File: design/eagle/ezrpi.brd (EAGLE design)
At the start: 65 x 56 mm, 40 parts, among them X1 26MHz, X2 32.768kHz, X3 48MHz

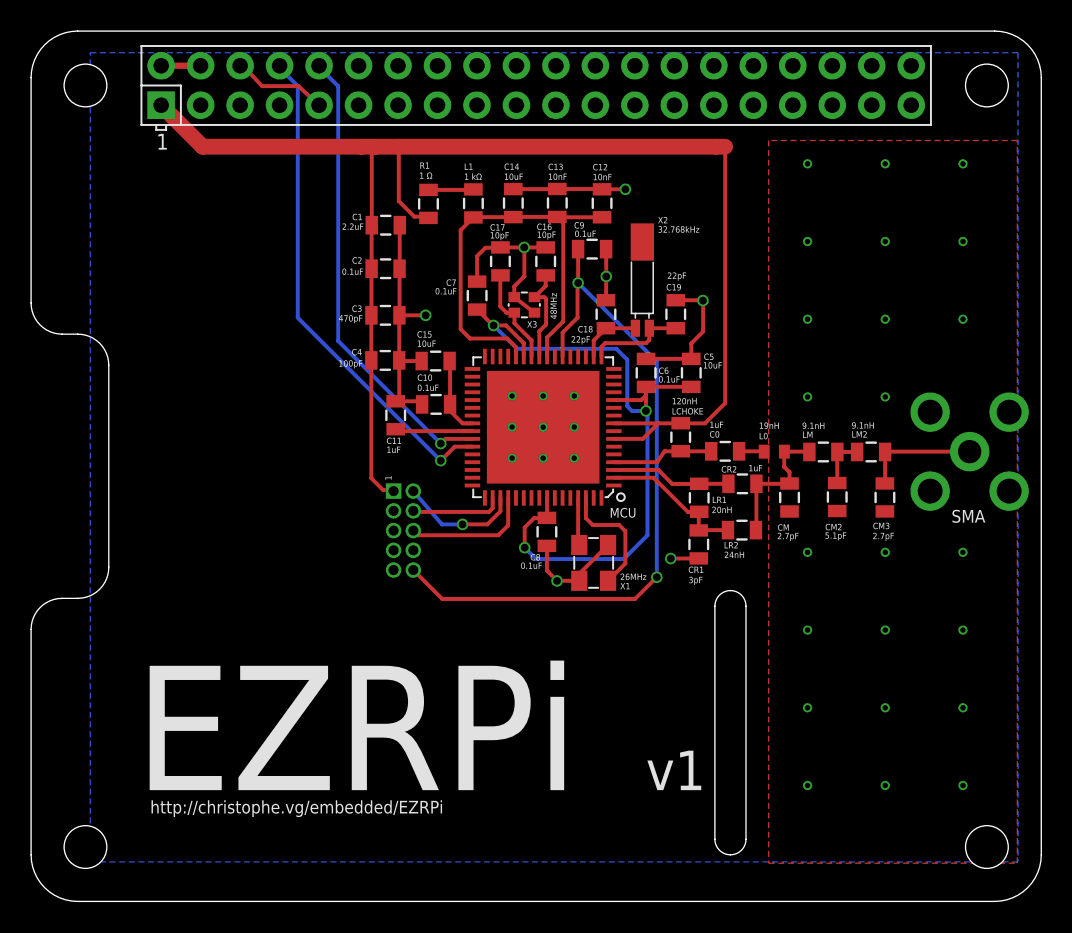
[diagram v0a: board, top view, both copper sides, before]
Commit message: added LEDs, improved traces, 50 Ω line, added vias
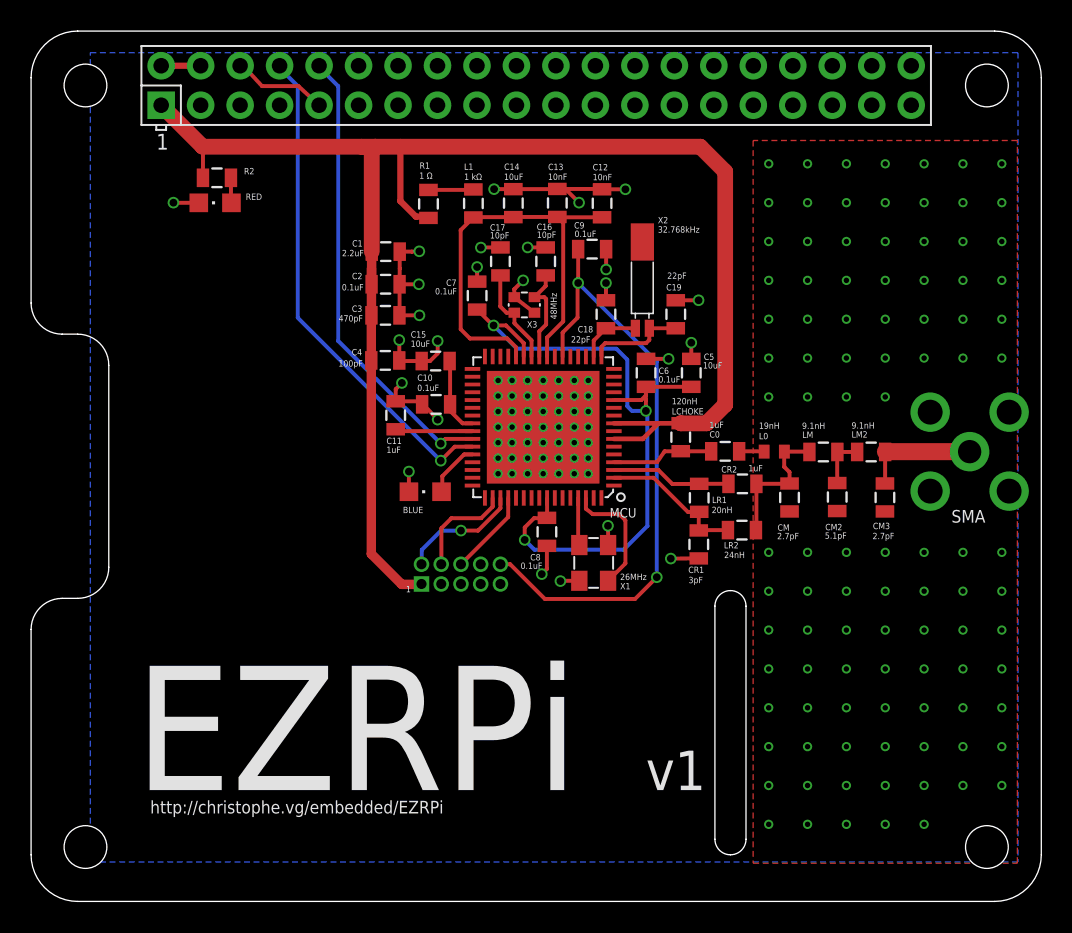
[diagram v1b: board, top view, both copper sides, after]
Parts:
- added BLUE, RED: (no value), led:CHIPLED_0805
- added R2: 68 Ω, passive:0805
- moved SWD 4.64 mm to (30.2, 23.6), turned to 0 degrees
- moved C1 1.70 mm to (25.4, 44.4)
- moved C2 1.00 mm to (25.4, 42.2)
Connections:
- new net LED-STATUS: BLUE.A, MCU.44
- new net N$8: R2.2, RED.A
- net GND: now also BLUE.C, RED.C
- net VCC: now also R2.1
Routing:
- net VCC: track 94.2 -> 109.5 mm
- net GND: track 62.2 -> 56.2 mm, vias 39 -> 174
- net RESET: track 45.4 -> 39.9 mm
- net LED-STATUS: track 0.00 -> 3.54 mm
- net SWO: track 8.25 -> 5.52 mm
- net N$8: track 0.00 -> 1.62 mm
- net IOVDD: track 46.4 -> 45.2 mm
- net SWCLK: track 5.89 -> 6.75 mm

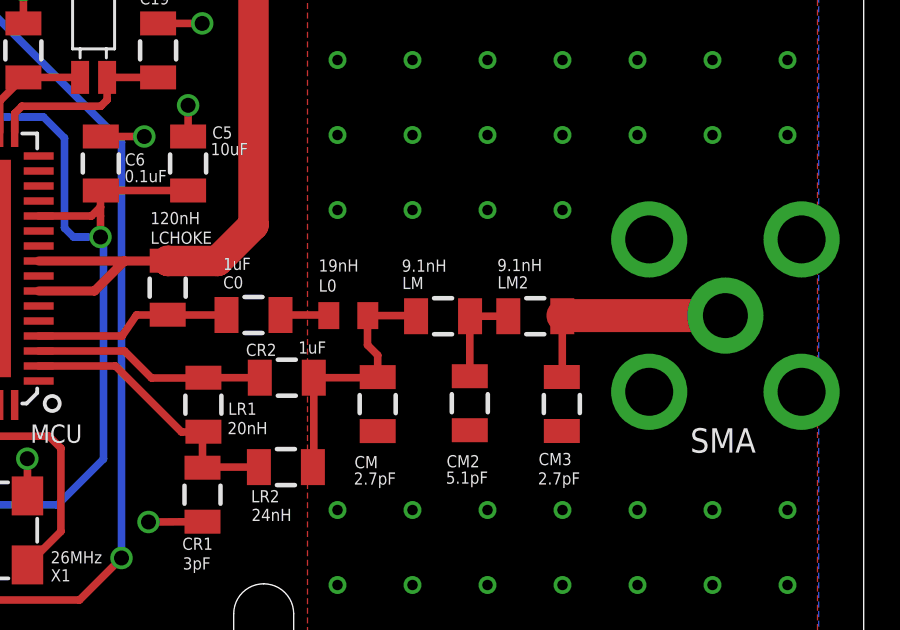
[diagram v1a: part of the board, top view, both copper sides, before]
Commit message: added more fence vias
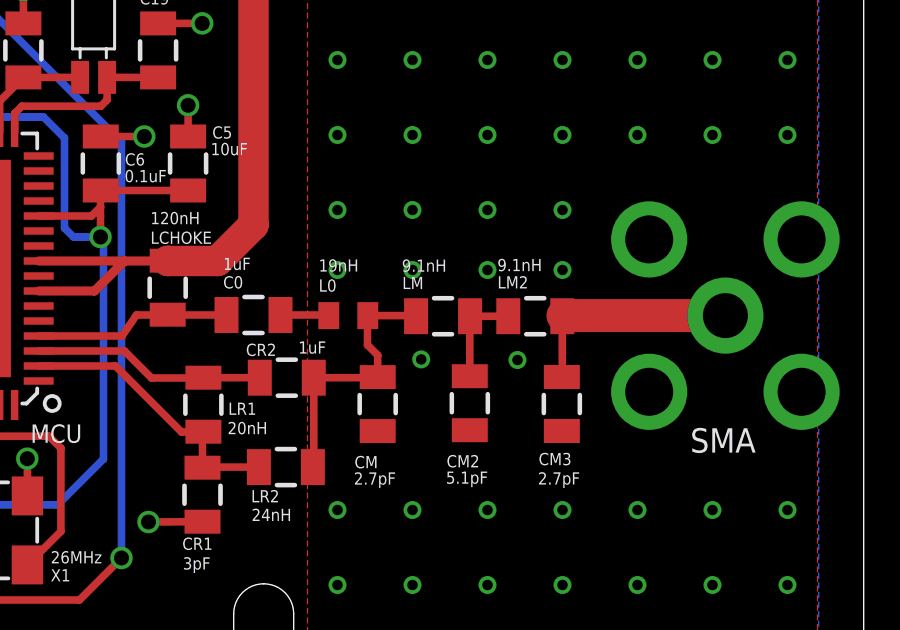
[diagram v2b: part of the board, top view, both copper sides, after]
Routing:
- net GND: vias 174 -> 180
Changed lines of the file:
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@@
 <via x="50" y="10" extent="1-16" drill="0.35" diameter="0.35"/>
 <via x="50" y="7.5" extent="1-16" drill="0.35" diameter="0.35"/>
+<via x="57.5" y="33" extent="1-16" drill="0.35" diameter="0.35"/>
+<via x="55" y="33" extent="1-16" drill="0.35" diameter="0.35"/>
+<via x="52.5" y="33" extent="1-16" drill="0.35" diameter="0.35"/>
+<via x="50" y="33" extent="1-16" drill="0.35" diameter="0.35"/>
+<via x="52.79" y="30.02" extent="1-16" drill="0.35" diameter="0.35"/>
+<via x="56" y="30" extent="1-16" drill="0.35" diameter="0.35"/>
 </signal>
 <signal name="RESET">
